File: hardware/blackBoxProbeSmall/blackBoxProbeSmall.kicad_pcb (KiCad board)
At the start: 4 copper layers, 44 x 29 mm, 75 parts, among them J1 USB-ID, J2 JTAG_2X05, J3 JTAG_2X05, J4 DevBoardUartInput, Q1 Q_NMOS_DUAL, Q2 Q_PMOS_DUAL, U1 MCP1702-MB, U2 USBLC6-2, U3 STM32F103CBT, U4 74X2T45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

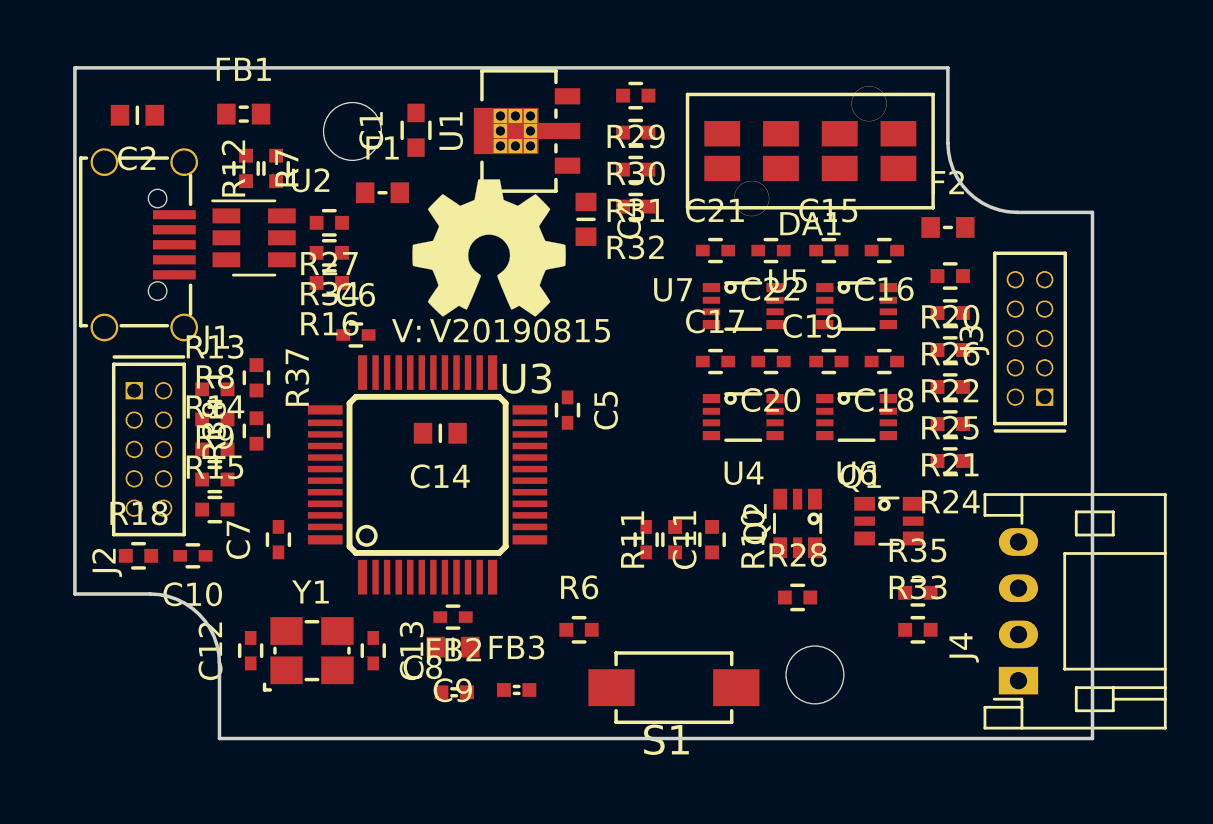
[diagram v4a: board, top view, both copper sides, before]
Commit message: component assignment, updated 3d models
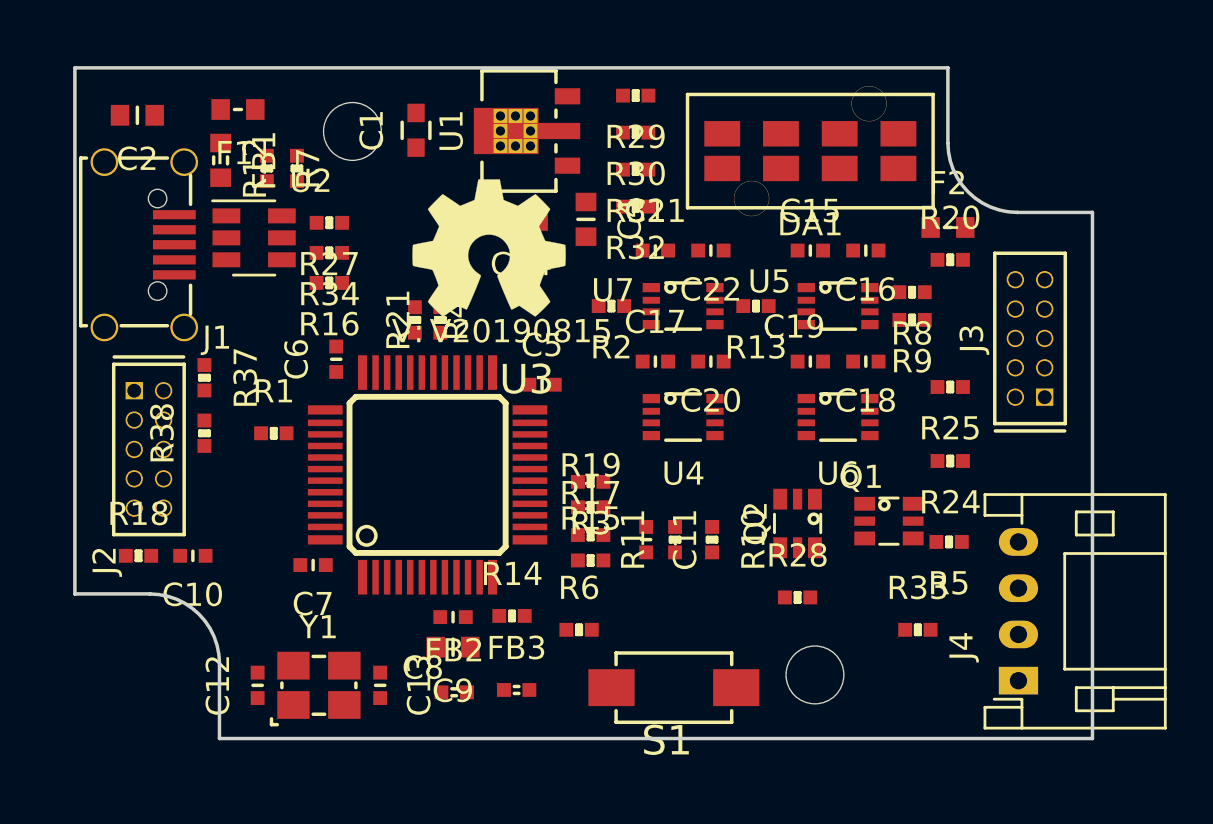
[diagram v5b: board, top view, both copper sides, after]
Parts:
- removed R22, R26, R35: 100, SquantorRcl:R_0402_hand
- added R1: 33, SquantorRcl:R_0402_hand, F.Cu at (132.3, 100.7)
- added R17: 33, SquantorRcl:R_0402_hand, F.Cu at (146.0, 105.1)
- added R19: 33, SquantorRcl:R_0402_hand, F.Cu at (146.0, 103.9)
- added R2: 33, SquantorRcl:R_0402_hand, F.Cu at (146.9, 95.2)
- added R3: 33, SquantorRcl:R_0402_hand, F.Cu at (146.0, 102.8)
- added R4: 33, SquantorRcl:R_0402_hand, F.Cu at (138.4, 95.8)
- added R5: 33, SquantorRcl:R_0402_hand, F.Cu at (161.5, 105.4)
- C11: value 100n -> 1uF
- R13, R14, R15, R21, R24, R25, R33, R8, R9: value 100 -> 33
- moved R9 30.9 mm to (159.9, 95.8), turned to 180 degrees
- moved R8 30.6 mm to (159.9, 94.6), turned to 180 degrees
- moved R13 23.7 mm to (153.2, 95.2), turned to 180 degrees
- moved R21 22.5 mm to (139.5, 95.8), turned to 90 degrees
- moved R15 16.4 mm to (146.0, 106.2)
- moved R14 14.7 mm to (142.6, 108.6)
- moved C14 9.84 mm to (143.0, 91.5)
- moved F1 7.21 mm to (130.8, 86.7), turned to 180 degrees
- moved C20 2.60 mm to (151.2, 97.6)
- moved C22 2.60 mm to (151.2, 92.8)
- moved C17 2.60 mm to (148.8, 97.6)
- moved C21 2.60 mm to (148.8, 92.8)
- moved U4 2.60 mm to (150.0, 100.0)
- moved U7 2.60 mm to (150.0, 95.2)
- moved R38 2.25 mm to (129.3, 100.7)
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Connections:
- J2 pad 10: Net-(J2-Pad10) -> /MCU_RST
- J2 pad 2: Net-(J2-Pad2) -> /MCU_TMS
- J2 pad 4: Net-(J2-Pad4) -> /MCU_TCK
- J2 pad 6: Net-(J2-Pad6) -> /MCU_TDO
- J2 pad 8: Net-(J2-Pad8) -> /MCU_TDI
- J3 pad 10: Net-(J3-Pad10) -> /PROBE_E_RST
- J3 pad 4: Net-(J3-Pad4) -> /PROBE_E_TCK
- J3 pad 8: Net-(J3-Pad8) -> /PROBE_E_TDI
- J4 pad 4: Net-(J4-Pad4) -> /PROBE_E_TX
- R13 pad 1: Net-(J2-Pad2) -> /PROBE_E_TMS
- R13 pad 2: /MCU_TMS -> Net-(R13-Pad2)
- R14 pad 1: Net-(J2-Pad6) -> Net-(R14-Pad1)
- R14 pad 2: /MCU_TDO -> /PROBE_TMS_DIR
- R15 pad 1: Net-(J2-Pad10) -> Net-(R15-Pad1)
- R15 pad 2: /MCU_RST -> /PROBE_I_TDI
- R21 pad 1: Net-(J3-Pad4) -> Net-(R21-Pad1)
- R21 pad 2: /PROBE_E_TCK -> /PROBE_I_TX
- R8 pad 1: Net-(J2-Pad4) -> /PROBE_E_TCK
- R8 pad 2: /MCU_TCK -> Net-(R8-Pad2)
- R9 pad 1: Net-(J2-Pad8) -> /PROBE_E_TDI
- R9 pad 2: /MCU_TDI -> Net-(R9-Pad2)
- U3 pad 11: /PROBE_TMS_DIR -> Net-(R14-Pad1)
- U3 pad 13: /PROBE_I_TDI -> Net-(R15-Pad1)
- U3 pad 14: /PROBE_I_TMS -> Net-(R17-Pad1)
- U3 pad 15: /PROBE_I_TCK -> Net-(R19-Pad1)
- U3 pad 30: /PROBE_I_TX -> Net-(R21-Pad1)
- U3 pad 39: /MCU_TDO -> Net-(R1-Pad1)
- U4 pad 6: /PROBE_E_TX -> Net-(R5-Pad2)
- U5 pad 6: /PROBE_E_TDI -> Net-(R9-Pad2)
- U5 pad 7: /PROBE_E_TCK -> Net-(R8-Pad2)
- U6 pad 2: /PROBE_I_TDO -> Net-(R3-Pad1)
- U6 pad 3: /PROBE_I_RX -> Net-(R4-Pad1)
- U7 pad 3: /PROBE_I_TMS -> Net-(R2-Pad1)
- U7 pad 6: /PROBE_E_TMS -> Net-(R13-Pad2)
